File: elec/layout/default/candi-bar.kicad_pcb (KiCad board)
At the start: 2 copper layers, 40 x 40 mm, 0 parts

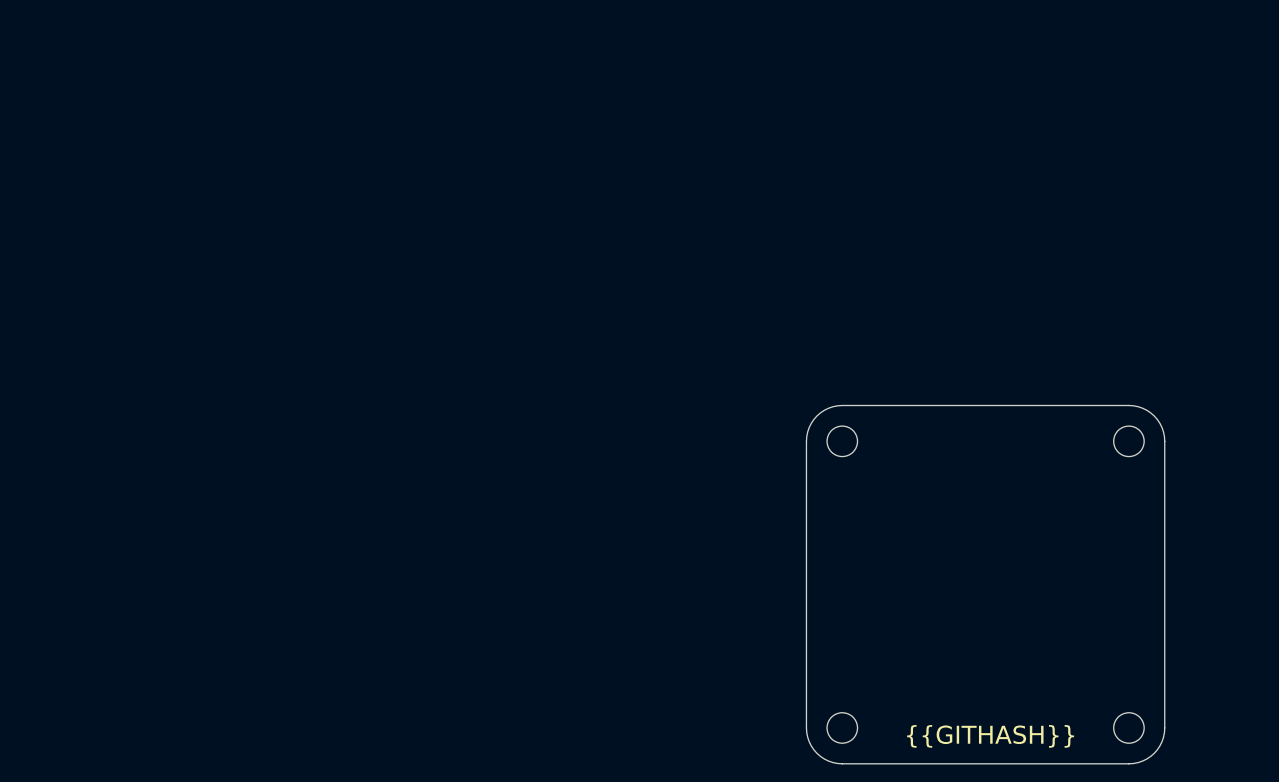
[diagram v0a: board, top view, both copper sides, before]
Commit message: feat: Initial attempt of CAN Hub
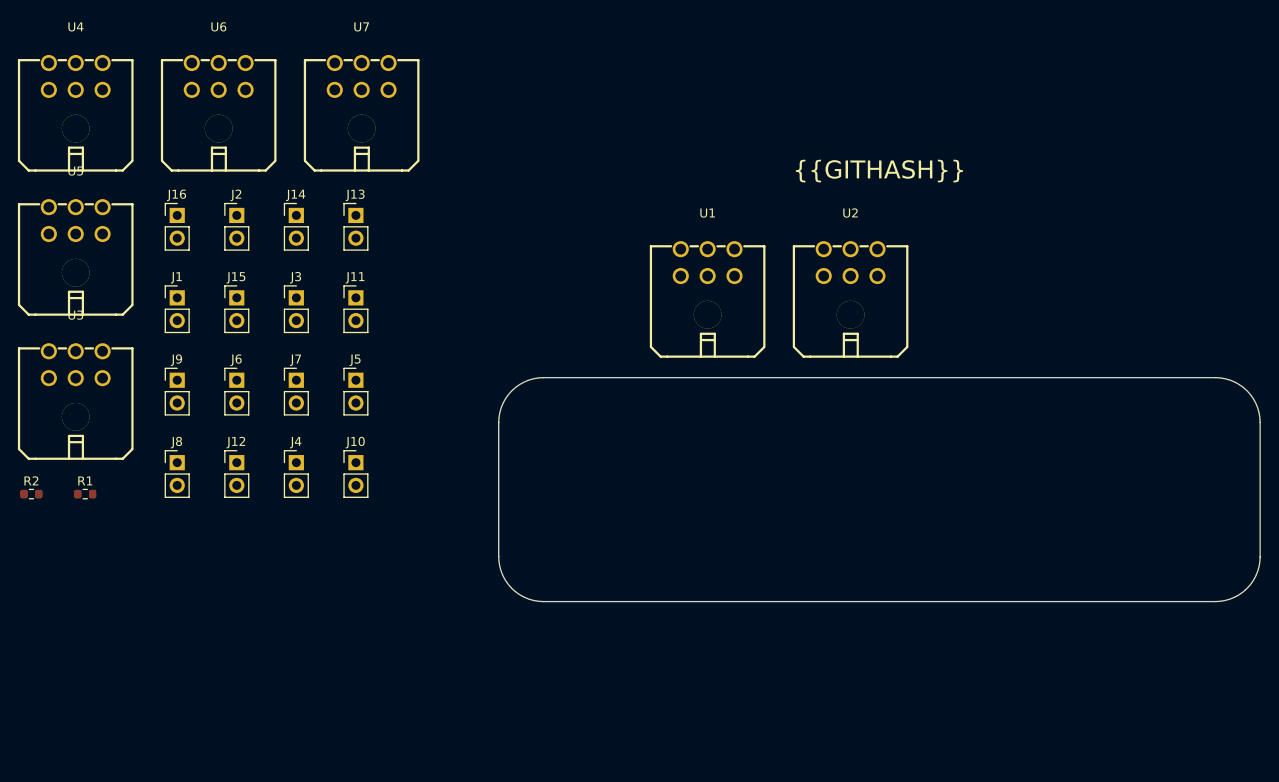
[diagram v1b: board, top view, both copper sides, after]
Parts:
- added J1: ?, lib:PinHeader_1x02_P2.54mm_Vertical, F.Cu at (59.1, 66.1)
- added J10: ?, lib:PinHeader_1x02_P2.54mm_Vertical, F.Cu at (79.1, 84.5)
- added J11: ?, lib:PinHeader_1x02_P2.54mm_Vertical, F.Cu at (79.1, 66.1)
- added J12: ?, lib:PinHeader_1x02_P2.54mm_Vertical, F.Cu at (65.8, 84.5)
- added J13: ?, lib:PinHeader_1x02_P2.54mm_Vertical, F.Cu at (79.1, 56.9)
- added J14: ?, lib:PinHeader_1x02_P2.54mm_Vertical, F.Cu at (72.4, 56.9)
- added J15: ?, lib:PinHeader_1x02_P2.54mm_Vertical, F.Cu at (65.8, 66.1)
- added J16: ?, lib:PinHeader_1x02_P2.54mm_Vertical, F.Cu at (59.1, 56.9)
- added J2: ?, lib:PinHeader_1x02_P2.54mm_Vertical, F.Cu at (65.8, 56.9)
- added J3: ?, lib:PinHeader_1x02_P2.54mm_Vertical, F.Cu at (72.4, 66.1)
- added J4: ?, lib:PinHeader_1x02_P2.54mm_Vertical, F.Cu at (72.4, 84.5)
- added J5: ?, lib:PinHeader_1x02_P2.54mm_Vertical, F.Cu at (79.1, 75.3)
- added J6: ?, lib:PinHeader_1x02_P2.54mm_Vertical, F.Cu at (65.8, 75.3)
- added J7: ?, lib:PinHeader_1x02_P2.54mm_Vertical, F.Cu at (72.4, 75.3)
- added J8: ?, lib:PinHeader_1x02_P2.54mm_Vertical, F.Cu at (59.1, 84.5)
- added J9: ?, lib:PinHeader_1x02_P2.54mm_Vertical, F.Cu at (59.1, 75.3)
- added R1: 100mW Thick Film Resistors 75V ±100ppm/℃ ±1% 120Ω 0603 Chip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, lib:R0603, F.Cu at (48.8, 88.0)
- added R2: 100mW Thick Film Resistors 75V ±100ppm/℃ ±1% 120Ω 0603 Chip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, lib:R0603, F.Cu at (42.8, 88.0)
- added U1: ?, lib:CONN-TH_43045-0600, F.Cu at (118.3, 62.2)
- added U2: ?, lib:CONN-TH_43045-0600, F.Cu at (134.3, 62.2)
- added U3: ?, lib:CONN-TH_43045-0600, F.Cu at (47.8, 73.6)
- added U4: ?, lib:CONN-TH_43045-0600, F.Cu at (47.8, 41.4)
- added U5: ?, lib:CONN-TH_43045-0600, F.Cu at (47.8, 57.5)
- added U6: ?, lib:CONN-TH_43045-0600, F.Cu at (63.7, 41.4)
- added U7: ?, lib:CONN-TH_43045-0600, F.Cu at (79.7, 41.4)
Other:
- board size 40 x 40 mm -> 85 x 25 mm
